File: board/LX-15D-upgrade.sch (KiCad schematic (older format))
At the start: 35 parts, among them J1 M+, J2 M-, J3 IN-1, J4 IN-2, U1 DRV8801RTY, U2 AS5600, U3 MPU-6050, U4 STM32L011F4Px, U5 AP7383-W5-3V3

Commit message: Route v0.1
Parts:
- removed C12: 10uF 16V, symbol Device:CP
- removed C5: 10u, symbol Device:C
- added J5: SWD, Connector_PinHeader_2.00mm:PinHeader_1x05_P2.00mm_Vertical, symbol Connector_Generic:Conn_01x05
- added R10, R9: 3k3, Resistor_SMD:R_0603_1608Metric_Pad1.05x0.95mm_HandSolder, symbol Device:R
- C1, C10, C11, C13, C14, C2, C3, C4, C6, C7, C8, C9: footprint (none) -> Capacitor_SMD:C_0603_1608Metric_Pad1.05x0.95mm_HandSolder
- D1: footprint VS-30BQ015HM3 -> Diode_SMD:D_2512_6332Metric
- D2, D3, D4: footprint (none) -> LED_SMD:LED_0603_1608Metric
- J1, J2: footprint (none) -> Connector_Pin:Pin_D1.0mm_L10.0mm
- J3, J4: footprint (none) -> Connector_Molex:Molex_Micro-Latch_53253-0370_1x03_P2.00mm_Vertical
- R1, R3, R4, R5, R6, R7, R8: footprint (none) -> Resistor_SMD:R_0603_1608Metric_Pad1.05x0.95mm_HandSolder
- R2: footprint (none) -> Resistor_SMD:R_2512_6332Metric_Pad1.52x3.35mm_HandSolder; #mfr (none) -> RCWE2512R100FKEA
- U1: value DRV8801RTY -> DRV8801A-Q1
- U5: footprint (none) -> Package_TO_SOT_SMD:SOT-23-5
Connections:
- net +3V3: now also J5.1 (Pin_1), R10.1, R9.1
- net BUS_VOLT: now also U4.11 (PA5); no longer U4.1 (PB9)
- net FAULT: now also U4.3 (PC15); no longer U4.11 (PA5)
- net GND: now also J3.3 (Pin_3), J4.3 (Pin_3), J5.5 (Pin_5); no longer J3.1 (Pin_1), J4.1 (Pin_1)
- net MODE1: now also U4.2 (PC14); no longer U4.3 (PC15)
- net PWR: now also U4.1 (PB9); no longer U4.2 (PC14)
- net RESET: now also J5.4 (Pin_4)
- net SCL: now also R9.2
- net SDA: now also R10.2
- net SWCLK: now also J5.3 (Pin_3)
- net SWDIO: now also J5.2 (Pin_2)
- net TX-RX: now also J3.1 (Pin_1), J4.1 (Pin_1); no longer J3.3 (Pin_3), J4.3 (Pin_3)
- net at U4.8 (PA2): now also D2.2 (A); no longer D3.2 (A)
- net at U4.9 (PA3): now also D3.2 (A); no longer D2.2 (A)
- net M+: now reaches J1.1 (Pin_1), U1.6 (OUT+)
- net M-: now reaches J2.1 (Pin_1), U1.9 (OUT-)
- net FSYNC: no longer names the net of U3.11 (FSYNC)
- no-connect marks 5 -> 6
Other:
- moved on the sheet: C13, C14, C2, C8, C9, D2, D3, D4, J1, J2, R6, R7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

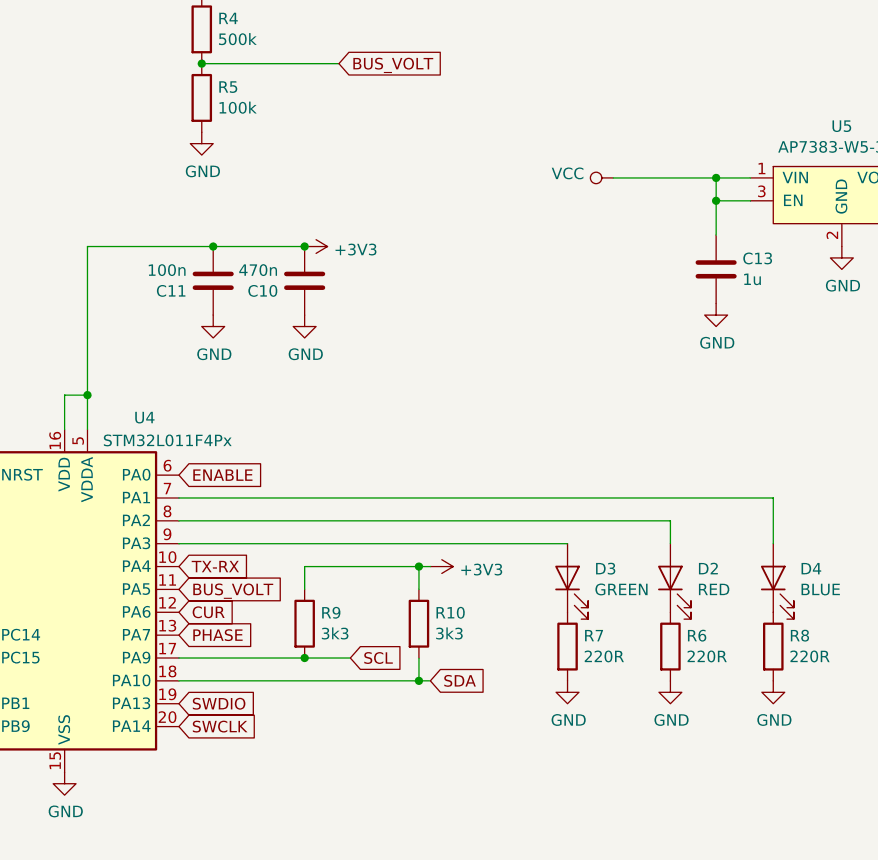
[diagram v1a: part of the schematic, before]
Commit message: Add power decoupling capacitor
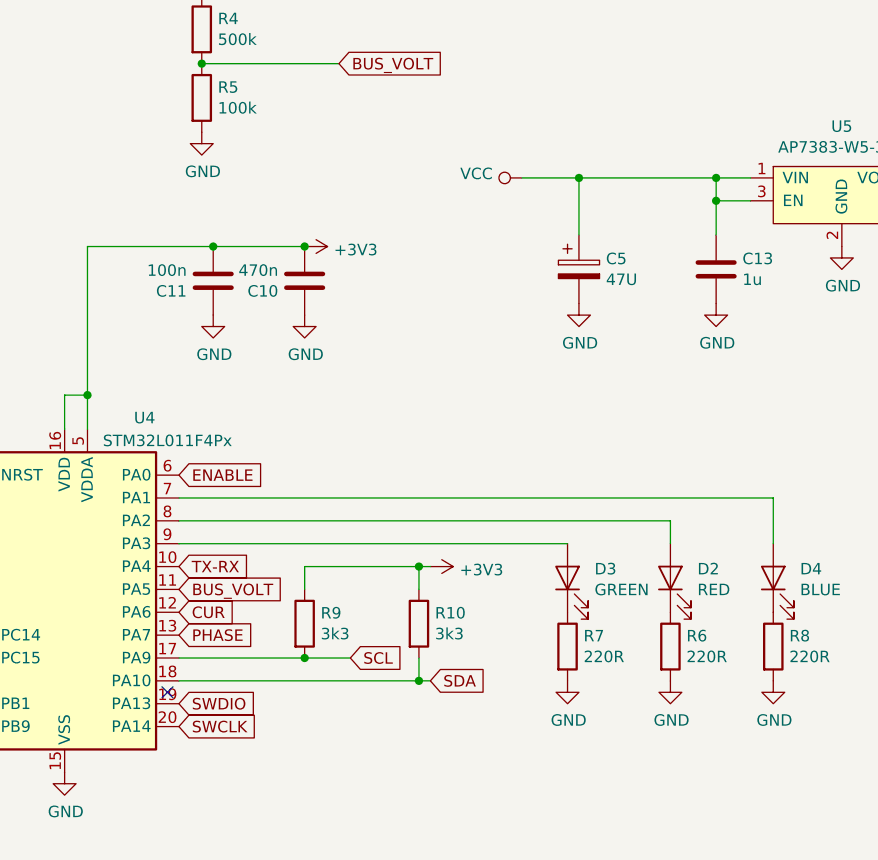
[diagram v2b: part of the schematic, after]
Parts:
- added C5: 47U, Capacitor_Tantalum_SMD:CP_EIA-6032-28_Kemet-C, symbol Device:CP
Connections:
- net GND: now also C5.2
- net VCC: now also C5.1
- no-connect marks 6 -> 7
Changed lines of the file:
@@
 L power:VCC #PWR0104
 U 1 1 5CA55269
-P 8150 1850
-F 0 "#PWR0104" H 8150 1700 50  0001 C CNN
-F 1 "VCC" V 8168 1977 50  0000 L CNN
-F 2 "" H 8150 1850 50  0001 C CNN
-F 3 "" H 8150 1850 50  0001 C CNN
-	1    8150 1850
+P 7750 1850
+F 0 "#PWR0104" H 7750 1700 50  0001 C CNN
+F 1 "VCC" V 7768 1977 50  0000 L CNN
+F 2 "" H 7750 1850 50  0001 C CNN
+F 3 "" H 7750 1850 50  0001 C CNN
+	1    7750 1850
 	0    -1   -1   0
 $EndComp
@@
 L power:GND #PWR0105
 U 1 1 5CA567F4
-P 8600 2400
-F 0 "#PWR0105" H 8600 2150 50  0001 C CNN
-F 1 "GND" H 8605 2227 50  0000 C CNN
-F 2 "" H 8600 2400 50  0001 C CNN
-F 3 "" H 8600 2400 50  0001 C CNN
-	1    8600 2400
+P 8000 2400
+F 0 "#PWR0105" H 8000 2150 50  0001 C CNN
+F 1 "GND" H 8005 2227 50  0000 C CNN
+F 2 "" H 8000 2400 50  0001 C CNN
+F 3 "" H 8000 2400 50  0001 C CNN
+	1    8000 2400
 	1    0    0    -1
 $EndComp
@@
 	6250 3350 8400 3350
 Wire Wire Line
-	8150 1850 8600 1850
+	7750 1850 8000 1850
 Wire Wire Line
 	3700 3250 3450 3250
@@
 Text Label 4200 3350 0    50   ~ 0
 M-
+$Comp
+L Device:CP C5
+U 1 1 5CAB6CAD
+P 8000 2250
+F 0 "C5" H 8118 2296 50  0000 L CNN
+F 1 "47U" H 8118 2205 50  0000 L CNN
+F 2 "Capacitor_Tantalum_SMD:CP_EIA-6032-28_Kemet-C" H 8038 2100 50  0001 C CNN
+F 3 "~" H 8000 2250 50  0001 C CNN
+F 4 "TAJC476K016SNJ" H 8000 2250 50  0001 C CNN "mfr#"
+	1    8000 2250
+	1    0    0    -1
+$EndComp
+$Comp
+L power:GND #PWR0111
+U 1 1 5CAC6A6C
+P 8600 2400
+F 0 "#PWR0111" H 8600 2150 50  0001 C CNN
+F 1 "GND" H 8605 2227 50  0000 C CNN
+F 2 "" H 8600 2400 50  0001 C CNN
+F 3 "" H 8600 2400 50  0001 C CNN
+	1    8600 2400
+	1    0    0    -1
+$EndComp
+Wire Wire Line
+	8000 2100 8000 1850
+Connection ~ 8000 1850
+Wire Wire Line
+	8000 1850 8600 1850
+NoConn ~ 6200 4100
 $EndSCHEMATC

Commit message: Final tweak
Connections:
- no-connect marks 7 -> 6
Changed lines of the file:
@@
 Wire Wire Line
 	8000 1850 8600 1850
-NoConn ~ 6200 4100
 $EndSCHEMATC
